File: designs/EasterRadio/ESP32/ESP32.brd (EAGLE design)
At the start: 54 x 67 mm, 25 parts, among them IC6 ESP32-WROVER-B, J3 S2B-NSHSS-TB, J5 S2B-NSHSS-TB

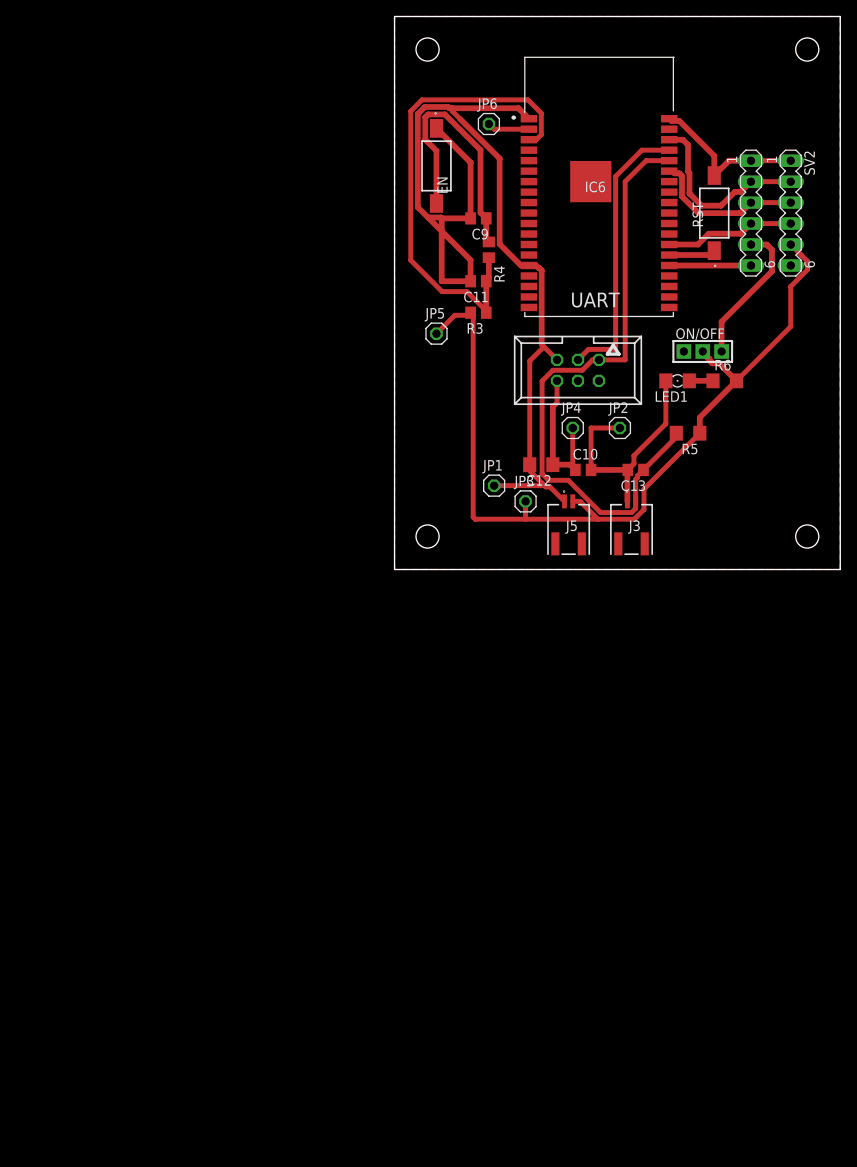
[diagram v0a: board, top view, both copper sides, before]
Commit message: added ESP32 wrover E schematic
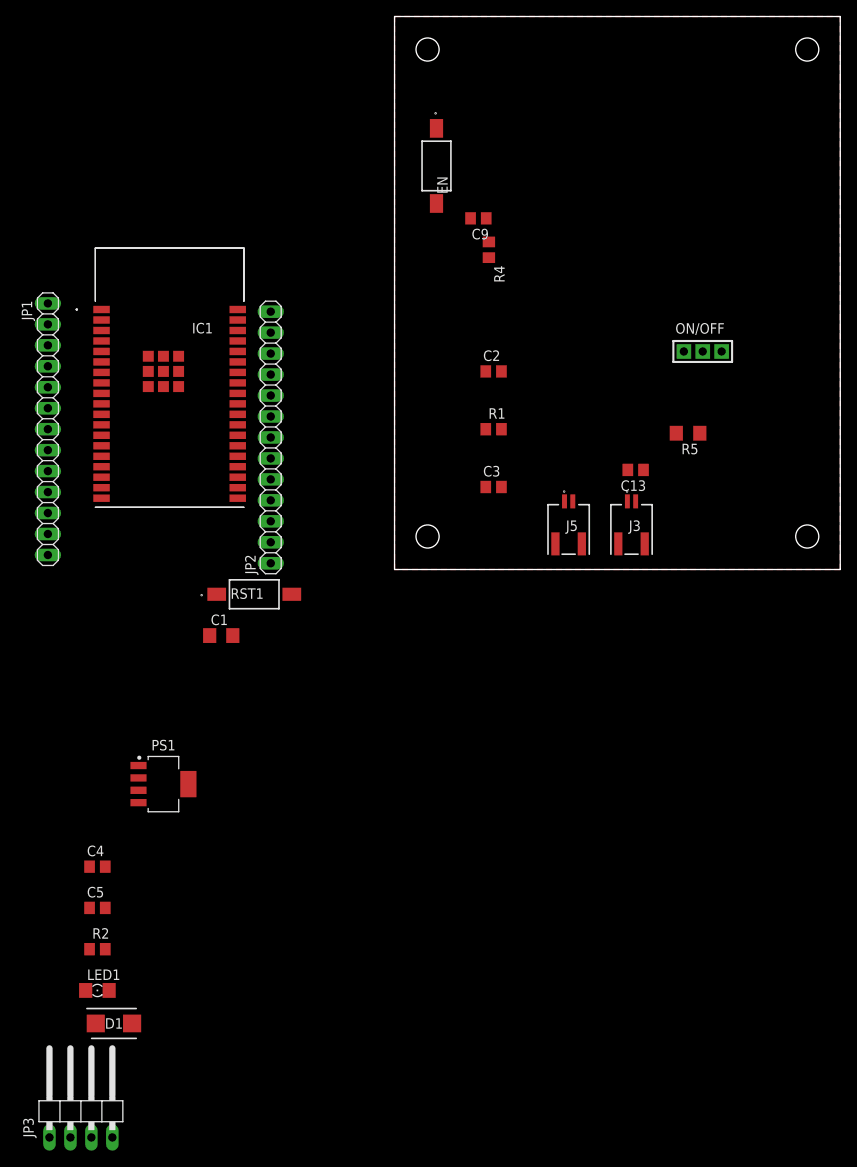
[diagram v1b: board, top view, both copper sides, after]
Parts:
- removed C10: 1uF, CommonParts:C0805
- removed C11: 1nF, CommonParts:C0805
- removed C12: 100uF, CommonParts:C1206
- removed IC6: ESP32-WROVER-B, ESP32-WROVER-B:ESP32WROVERIB16MB
- removed JP4, JP5, JP6: (no value), pinhead:1X01
- removed R3: 12k, CommonParts:R0805
- removed R6: 1K, rcl:R1206
- removed RST: FSMSMTR, FSMSMTR:FSMSM
- removed SV1, SV2: (no value), con-lstb:MA06-1
- removed UART: 057-006-1, con-panduit:057-006-1
- added C1: 100uF, CommonParts:C1206
- added C2: 1uF, CommonParts:C0805
- added C3: 1nF, CommonParts:C0805
- added C4, C5: (no value), rcl:C0805
- added D1: LSM115JE3_TR13, CommonParts:DIOM5436X330N
- added IC1: ESP32-WROVER-E, MouserUseful:ESP32WROVERBM213DH6464PC3Q0
- added PS1: LP38693MPX-5.0_NOPB, MouserUseful:SOT150P700X160-5N
- added R1: 12k, CommonParts:R0805
- added R2: (no value), rcl:R0805
- added RST1: FSMSMTR, FSMSMTR:FSMSM
- JP1, JP2: device pinhead:1X01 -> pinhead:1X13
- JP3: device pinhead:1X01 -> pinhead:1X04/90
- LED1: device led:1206 -> CommonParts:1206
- moved LED1 102.0 mm to (-36.0, -51.0), turned to 0 degrees
- moved JP3 90.9 mm to (-38.0, -65.0)
- moved JP1 54.5 mm to (-42.0, 17.0), turned to 270 degrees
- moved JP2 42.3 mm to (-15.0, 16.0), turned to 90 degrees
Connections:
- removed net 3.3V_IN: ON/OFF.P$1, SV1.5
- removed net CLK: IC6.20
- removed net CMD: IC6.19
- removed net GPIO12: IC6.14
- removed net GPIO13: IC6.16
- removed net GPIO14: IC6.13
- removed net GPIO15: IC6.23
- removed net IO0: IC6.25, RST.1
- removed net IRQ: IC6.26, SV1.4, SV2.4
- removed net N$14: LED1.A, R6.1
- removed net NC_1: IC6.27
- removed net NC_2: IC6.28
- removed net NC_3: IC6.32
- removed net RST: IC6.24, SV1.6
- removed net SCLK: IC6.36, SV1.2, SV2.2
- removed net SD0: IC6.21
- removed net SD1: IC6.22
- removed net SD2: IC6.17
- removed net SD3: IC6.18
- removed net SDIO: IC6.33, SV1.3, SV2.3
- removed net SEN_VN: IC6.5
- removed net SEN_VP: IC6.4
- new net 3.3VOUT: C4.1, PS1.3, R2.1
- new net EN3.3V: ON/OFF.P$2, PS1.1
- new net IO1: IC1.25, RST1.1
- new net IO12: IC1.14, JP1.13
- new net IO14: IC1.13, JP1.12
- new net IO15: IC1.23, JP2.1
- new net IO16: IC1.27, JP2.4
- new net IO17: IC1.28, JP2.5
- new net IO2: IC1.24, JP2.2
- new net IO21: IC1.33, JP2.9
- new net IO22: IC1.36, JP2.12
- new net IO4: IC1.26, JP2.3
- new net N$1: LED1.A, R2.2
- new net SENSOR_VN: IC1.5, JP1.4
- new net SENSOR_VP: IC1.4, JP1.3
- net 3.3V: now also C1.1, C2.1, C5.1, D1.1, IC1.2, JP1.2, ON/OFF.P$3, PS1.4, R1.2; no longer C10.1, C12.1, IC6.2, JP4.1, JP5.1, JP6.1, ON/OFF.P$2, R3.2, R6.2, SV2.5, UART.6
- net EN: now also C3.1, IC1.3, R1.1; no longer C11.1, IC6.3, R3.1
- net GND: now also C1.2, C2.2, C3.2, C4.2, C5.2, D1.2, IC1.1, IC1.15, IC1.38, IC1.39, IC1.40, IC1.41, IC1.42, IC1.43, IC1.44, IC1.45, IC1.46, IC1.47, JP3.2, ON/OFF.P$1, PS1.5, RST1.2; no longer C10.2, C11.2, C12.2, IC6.1, IC6.15, IC6.38, IC6.39, JP2.1, RST.2, SV1.1, SV2.1, UART.5
- net IO18: now also IC1.30, JP2.7; no longer IC6.30
- net IO19: now also IC1.31, JP2.8; no longer IC6.31
- net IO23: now also IC1.37, JP2.13; no longer IC6.37
- net IO25: now also IC1.10, JP1.9; no longer IC6.10
- net IO26: now also IC1.11, JP1.10; no longer IC6.11
- net IO27: now also IC1.12, JP1.11; no longer IC6.12
- net IO32: now also IC1.8, JP1.7; no longer IC6.8
- net IO33: now also IC1.9, JP1.8; no longer IC6.9
- net IO34: now also IC1.6, JP1.5; no longer IC6.6
- net IO35: now also IC1.7, JP1.6; no longer IC6.7
- net IO5: now also IC1.29, JP2.6; no longer IC6.29
- net RXD0: now also IC1.34, JP2.10, JP3.4; no longer IC6.34, UART.1
- net TXD0: now also IC1.35, JP2.11, JP3.3; no longer IC6.35, UART.3
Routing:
- net GND: track 179.9 -> 0.00 mm
- net 3.3V: track 128.6 -> 0.00 mm
- net RXD0: track 75.1 -> 0.00 mm
- net EN: track 58.2 -> 0.00 mm
- net TXD0: track 33.8 -> 0.00 mm
- net EN_1: track 31.7 -> 0.00 mm
- net SCLK: track 22.6 -> 0.00 mm
- net SDIO: track 18.8 -> 0.00 mm
- net 3.3V_IN: track 17.6 -> 0.00 mm
- net IRQ: track 15.8 -> 0.00 mm
- net RST: track 9.90 -> 0.00 mm
- net IO0: track 5.67 -> 0.00 mm
- net N$14: track 2.87 -> 0.00 mm

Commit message: added STM32 CAN to RS232 Adapter
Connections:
- net 3.3V: no longer C1.1, C2.1, IC1.2, R1.2
- net 3.3VOUT: now also C1.1, C2.1, IC1.2, R1.2
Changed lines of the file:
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@@
 <contactref element="R5" pad="1"/>
 <contactref element="J5" pad="2"/>
-<contactref element="C1" pad="1"/>
-<contactref element="IC1" pad="2"/>
-<contactref element="C2" pad="1"/>
-<contactref element="R1" pad="2"/>
 <contactref element="ON/OFF" pad="P$3"/>
 <contactref element="PS1" pad="4"/>
@@
 <wire x1="-36.95" y1="-41" x2="-36.2" y2="-55" width="0" layer="19" extent="1-1"/>
 <wire x1="-31.0226" y1="-28.25" x2="-36.95" y2="-41" width="0" layer="19" extent="1-1"/>
-<wire x1="-22.4" y1="-8" x2="-31.0226" y2="-28.25" width="0" layer="19" extent="1-1"/>
-<wire x1="-35.5" y1="30.23" x2="-22.4" y2="-8" width="0" layer="19" extent="1-1"/>
-<wire x1="-42" y1="29.7" x2="-35.5" y2="30.23" width="0" layer="19" extent="1-1"/>
-<wire x1="12.95" y1="17" x2="-22.4" y2="-8" width="0" layer="19" extent="1-1"/>
-<wire x1="11.05" y1="24" x2="12.95" y2="17" width="0" layer="19" extent="1-1"/>
-<wire x1="21.59" y1="8.255" x2="12.95" y2="17" width="0" layer="19" extent="1-1"/>
+<wire x1="-42" y1="29.7" x2="-31.0226" y2="-28.25" width="0" layer="19" extent="1-1"/>
+<wire x1="21.59" y1="8.255" x2="-31.0226" y2="-28.25" width="0" layer="19" extent="1-1"/>
 <wire x1="36.982" y1="16.51" x2="21.59" y2="8.255" width="0" layer="19" extent="1-1"/>
 <wire x1="35.052" y1="26.416" x2="36.982" y2="16.51" width="0" layer="19" extent="1-1"/>
@@
 <contactref element="C4" pad="1"/>
 <contactref element="R2" pad="1"/>
+<contactref element="C1" pad="1"/>
+<contactref element="IC1" pad="2"/>
+<contactref element="C2" pad="1"/>
+<contactref element="R1" pad="2"/>
 <wire x1="-36.95" y1="-36" x2="-36.95" y2="-46" width="0" layer="19" extent="1-1"/>
 <wire x1="-31.0226" y1="-26.75" x2="-36.95" y2="-36" width="0" layer="19" extent="1-1"/>
+<wire x1="-22.4" y1="-8" x2="-31.0226" y2="-26.75" width="0" layer="19" extent="1-1"/>
+<wire x1="-35.5" y1="30.23" x2="-22.4" y2="-8" width="0" layer="19" extent="1-1"/>
+<wire x1="12.95" y1="17" x2="-22.4" y2="-8" width="0" layer="19" extent="1-1"/>
+<wire x1="11.05" y1="24" x2="12.95" y2="17" width="0" layer="19" extent="1-1"/>
 </signal>
 <signal name="N$1">

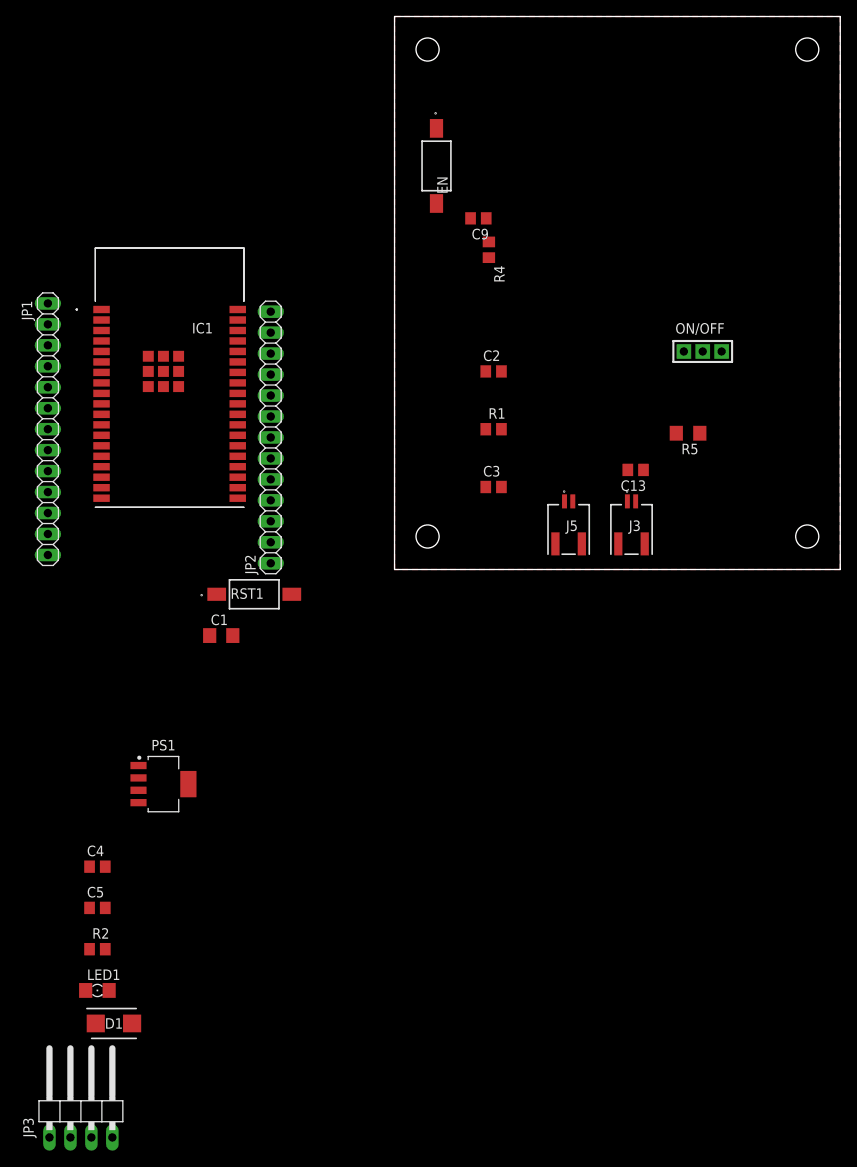
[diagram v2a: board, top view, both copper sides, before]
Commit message: ESP32 brd layout
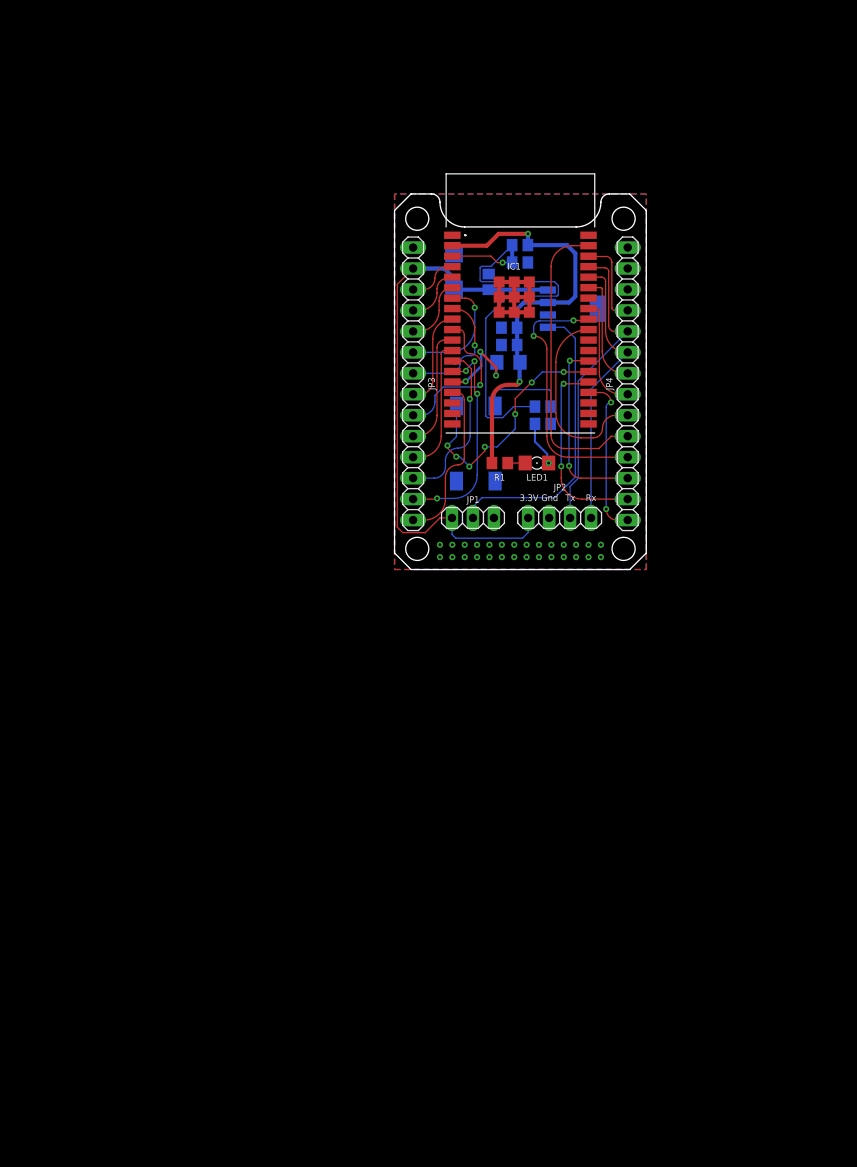
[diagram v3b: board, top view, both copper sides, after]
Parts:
- removed C13: 20nF, CommonParts:C0805
- removed C9: 1nF, CommonParts:C0805
- removed EN, RST1: FSMSMTR, FSMSMTR:FSMSM
- removed J3, J5: S2B-NSHSS-TB, CommonParts:SM02B-NSHSS-TB
- removed ON/OFF: -CON3, tango:CON3
- removed R4: 460ohm, CommonParts:R0805
- removed R5: 10K, CommonParts:R1206
- added C6: 1nF, CommonParts:C0805
- added JP4: (no value), pinhead:1X14
- added R3: 460ohm, CommonParts:R0805
- added S1, S2: FSMSMTR, FSMSMTR:FSMSM
- C2: value 1uF -> (none); device CommonParts:C0805 -> rcl:C0805
- C3: value 1nF -> 1uF
- C4: value (none) -> 1nF; device rcl:C0805 -> CommonParts:C0805
- JP1: device pinhead:1X13 -> pinhead:1X03
- JP2: device pinhead:1X13 -> pinhead:1X04
- JP3: device pinhead:1X04/90 -> pinhead:1X14
- R1: value 12k -> (none); device CommonParts:R0805 -> rcl:R0805
- R2: value (none) -> 12k; device rcl:R0805 -> CommonParts:R0805
- moved D1 100.0 mm to (7.20, 36.1), flipped to the bottom, turned to 90 degrees
- moved R2 99.5 mm to (15.2, 39.3), flipped to the bottom, turned to 180 degrees
- moved JP3 96.3 mm to (2.25, 22.5), turned to 270 degrees
- moved C5 89.4 mm to (11.4, 34.9), flipped to the bottom, turned to 90 degrees
- moved C4 89.3 mm to (15.2, 37.2), flipped to the bottom, turned to 180 degrees
- moved LED1 83.2 mm to (17.2, 12.9)
- moved PS1 76.0 mm to (21.6, 31.6), flipped to the bottom, turned to 180 degrees
- moved JP1 52.6 mm to (9.50, 6.25), turned to 0 degrees
- moved C1 48.0 mm to (13.8, 25.1), flipped to the bottom
- moved IC1 43.4 mm to (14.5, 33.0)
- moved JP2 36.3 mm to (20.0, 6.25), turned to 0 degrees
- moved C3 17.3 mm to (13.9, 27.2), flipped to the bottom
- moved C2 5.63 mm to (13.9, 29.3), flipped to the bottom
- moved R1 4.17 mm to (12.8, 12.9)
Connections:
- removed net IO15: IC1.23, JP2.1
- removed net IO16: IC1.27, JP2.4
- removed net IO17: IC1.28, JP2.5
- removed net IO18: IC1.30, JP2.7
- removed net IO19: IC1.31, JP2.8
- removed net IO2: IC1.24, JP2.2
- removed net IO23: IC1.37, JP2.13
- removed net IO4: IC1.26, JP2.3
- removed net IO5: IC1.29, JP2.6
- new net CS: IC1.23, JP4.1
- new net DC: IC1.24, JP4.2
- new net ENC_1: IC1.29, JP4.6
- new net ENC_2: IC1.31, JP4.7
- new net IO13: IC1.16, JP3.14
- new net MOSI: IC1.37, JP4.5
- new net RST: IC1.26, JP4.3
- new net SCLK: IC1.30, JP4.4
- net 3.3V: now also JP1.1, JP2.1, JP3.2; no longer J5.2, JP1.2, JP3.1, ON/OFF.P$3, R5.1
- net 3.3VOUT: now also C3.1, R1.1, R2.2; no longer C4.1, R1.2, R2.1
- net EN: now also C4.1, R2.1, R3.2; no longer C3.1, R1.1, R4.2
- net EN3.3V: now also JP1.2; no longer ON/OFF.P$2
- net EN_1: now also C6.1, R3.1, S2.2; no longer C9.1, EN.2, R4.1
- net GND: now also C6.2, JP1.3, JP2.2, JP3.1, S1.1, S2.1; no longer C13.2, C9.2, EN.1, J3.1, J5.1, JP1.1, JP3.2, ON/OFF.P$1, RST1.2
- net IO1: now also S1.2; no longer RST1.1
- net IO12: now also JP3.13; no longer JP1.13
- net IO14: now also JP3.12; no longer JP1.12
- net IO21: now also JP4.8; no longer JP2.9
- net IO22: now also JP4.11; no longer JP2.12
- net IO25: now also JP3.9; no longer JP1.9
- net IO26: now also JP3.10; no longer JP1.10
- net IO27: now also JP3.11; no longer JP1.11
- net IO32: now also JP3.7; no longer JP1.7
- net IO33: now also JP3.8; no longer JP1.8
- net IO34: now also JP3.5; no longer JP1.5
- net IO35: now also JP3.6; no longer JP1.6
- net N$1: now also R1.2; no longer R2.2
- net RXD0: now also JP2.4, JP4.9; no longer C13.1, J3.2, JP2.10, JP3.4, R5.2
- net SENSOR_VN: now also JP3.4; no longer JP1.4
- net SENSOR_VP: now also JP3.3; no longer JP1.3
- net TXD0: now also JP2.3, JP4.10; no longer JP2.11, JP3.3
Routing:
- net 3.3V: track 0.00 -> 71.9 mm
- net EN: track 0.00 -> 55.5 mm, vias 0 -> 1
- net 3.3VOUT: track 0.00 -> 51.0 mm, vias 0 -> 2
- net GND: track 0.00 -> 38.9 mm, vias 0 -> 32
- net TXD0: track 0.00 -> 37.3 mm
- net MOSI: track 0.00 -> 36.7 mm
- net EN3.3V: track 0.00 -> 35.9 mm
- net RXD0: track 0.00 -> 34.0 mm
- net SCLK: track 0.00 -> 31.8 mm, vias 0 -> 2
- net IO1: track 0.00 -> 30.8 mm, vias 0 -> 7
- net IO12: track 0.00 -> 26.4 mm, vias 0 -> 4
- net DC: track 0.00 -> 23.8 mm, vias 0 -> 2
- net ENC_1: track 0.00 -> 22.8 mm
- net RST: track 0.00 -> 22.8 mm, vias 0 -> 2
- net IO14: track 0.00 -> 21.0 mm, vias 0 -> 1
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- added copper zone on layer 16, net GND
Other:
- board size 54 x 67 mm -> 30.5 x 45.5 mm
- board text added: "3.3V"
- board text added: "Gnd"
- board text added: "Rx"
- board text added: "Tx"
